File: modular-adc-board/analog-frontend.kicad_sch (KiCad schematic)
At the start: 101 parts, among them J1001 BWU.FL-IPEX1, J1002 BWU.FL-IPEX1, J1003 BWU.FL-IPEX1, J1004 BWU.FL-IPEX1, J1005 BWU.FL-IPEX1, J1006 BWU.FL-IPEX1, J1007 8P8C_Shielded, J1008 BWU.FL-IPEX1, J1009 BWU.FL-IPEX1, J1010 BWU.FL-IPEX1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

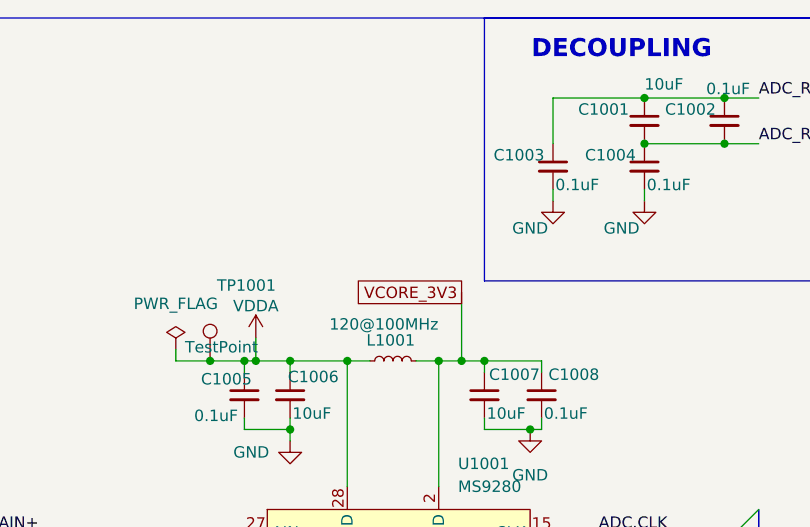
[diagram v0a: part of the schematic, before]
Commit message: minor board changes, notes on double-adc usage, added simulations
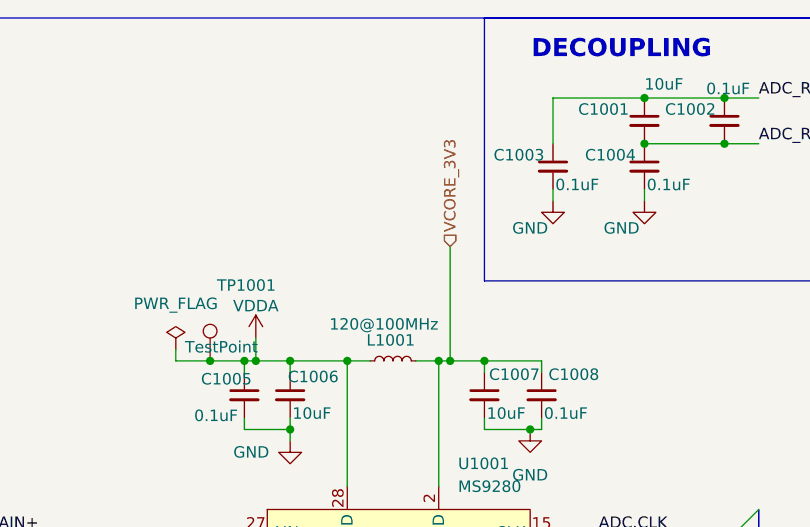
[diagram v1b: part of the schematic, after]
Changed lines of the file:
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@@
 	)
 	(junction
-		(at 361.95 52.07)
+		(at 337.82 52.07)
 		(diameter 0)
 		(color 0 0 0 0)
 	)
 	(junction
-		(at 337.82 52.07)
+		(at 360.68 52.07)
 		(diameter 0)
 		(color 0 0 0 0)
@@
 	(wire
 		(pts
-			(xy 361.95 52.07) (xy 364.49 52.07)
-		)
-		(stroke
-			(width 0)
-			(type default)
-		)
-	)
-	(wire
-		(pts
 			(xy 189.23 99.06) (xy 189.23 97.79)
 		)
@@
 	(wire
 		(pts
-			(xy 361.95 44.45) (xy 361.95 52.07)
+			(xy 360.68 39.37) (xy 360.68 52.07)
 		)
 		(stroke
@@
 	(wire
 		(pts
-			(xy 359.41 52.07) (xy 361.95 52.07)
+			(xy 359.41 52.07) (xy 360.68 52.07)
 		)
 		(stroke
@@
 	(wire
 		(pts
+			(xy 360.68 52.07) (xy 364.49 52.07)
+		)
+		(stroke
+			(width 0)
+			(type default)
+		)
+	)
+	(wire
+		(pts
 			(xy 172.72 92.71) (xy 172.72 113.03)
 		)
@@
 		)
 	)
-	(global_label "VCORE_3V3"
-		(shape passive)
-		(at 361.95 44.45 180)
-		(fields_autoplaced yes)
+	(hierarchical_label "VCORE_3V3"
+		(shape input)
+		(at 360.68 39.37 90)
 		(effects
 			(font
 				(size 1.27 1.27)
 			)
-			(justify right)
-		)
-		(property "Intersheetrefs" "${INTERSHEET_REFS}"
-			(at 349.4928 44.45 0)
-			(effects
-				(font
-					(size 1.27 1.27)
-				)
-				(justify right)
-				(hide yes)
-			)
+			(justify left)
 		)
 	)
